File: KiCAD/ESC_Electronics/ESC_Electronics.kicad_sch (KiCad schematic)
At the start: 68 parts, among them J1 Batt probe, J10 RV Prob, J2 CA probe, J3 Test Input BNC, J4 -1000VDC SHV, J5 Output BNC, J6 Barrel_Jack, J7 DC Power, J8 -8V, J9 +8V, U1 CR110, U2 SiPhotodiode, U3 TL051CP, U4 LM317L, U5 UA78M08, U6 UA79M08, U7 TLE2426xP

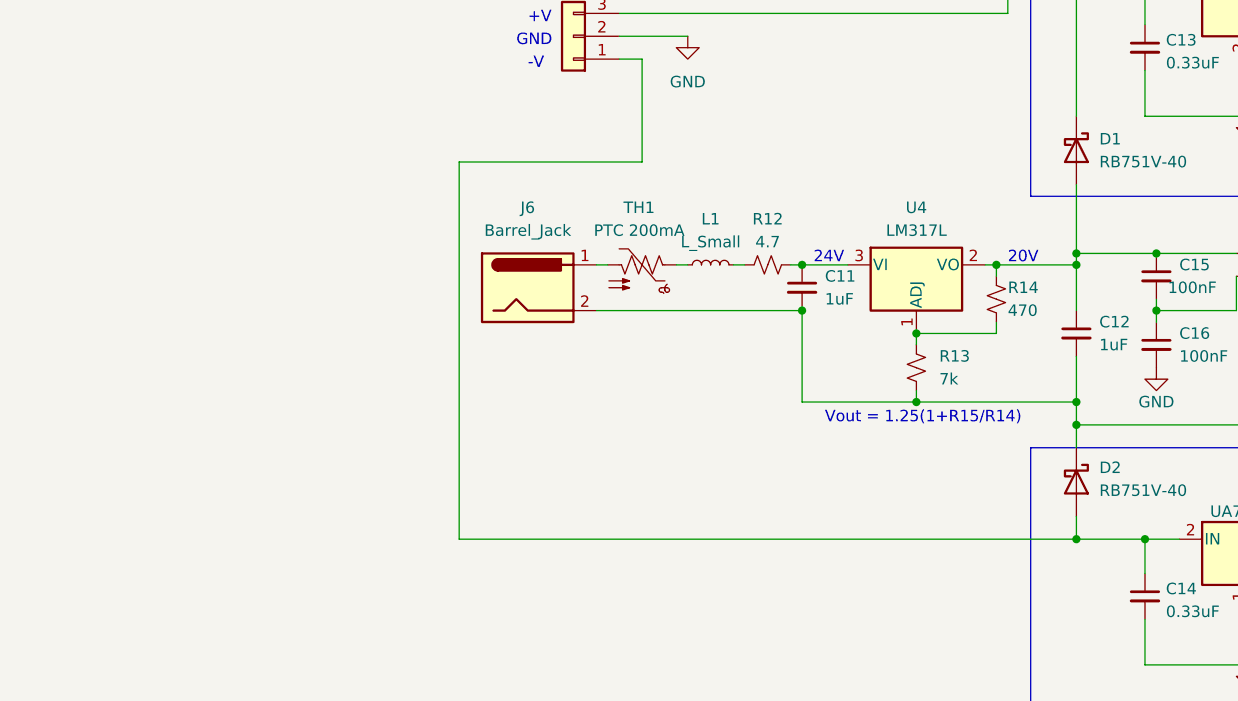
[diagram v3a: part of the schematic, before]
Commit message: Cleaning up SCH w/ notes
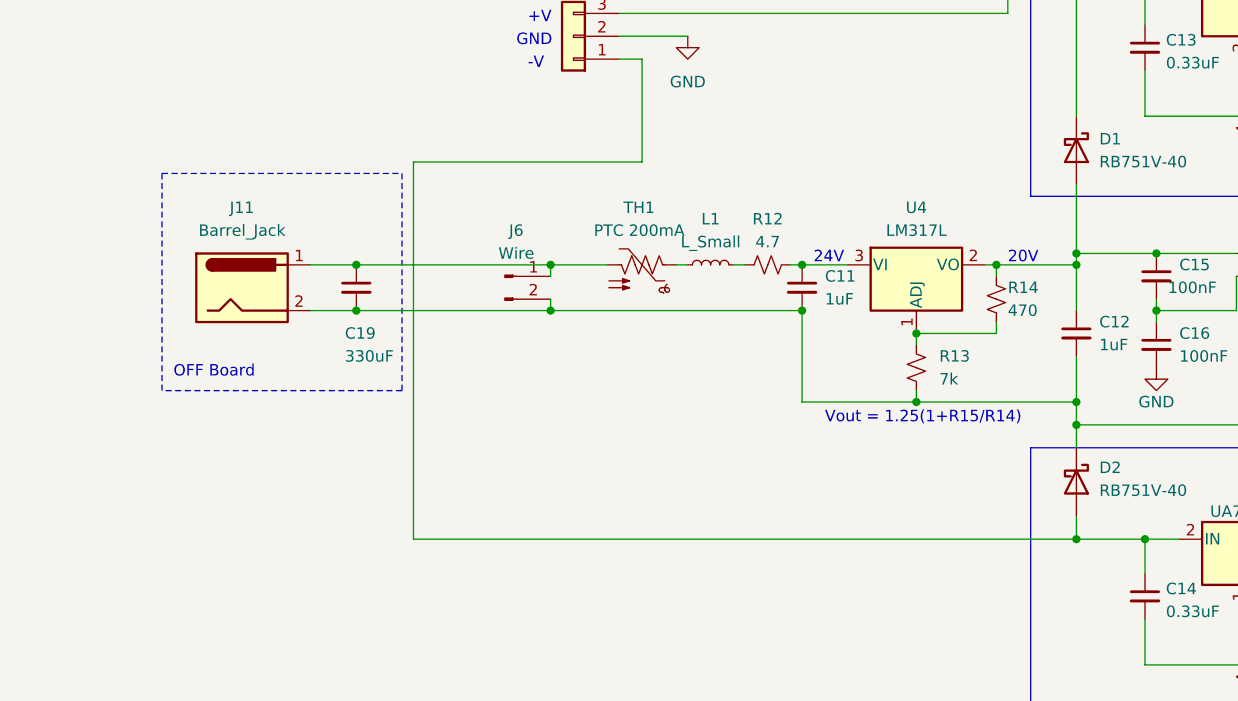
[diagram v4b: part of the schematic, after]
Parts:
- added C19: 330uF, symbol Device:C_Small
- added J11: Barrel_Jack, Connector_PinHeader_2.54mm:PinHeader_1x02_P2.54mm_Vertical, symbol Connector:Barrel_Jack
- J6: value Barrel_Jack -> Wire; symbol Connector:Barrel_Jack -> Connector:Conn_01x02_Pin; Digikey 839-1580-ND -> (none)
- R3: Digikey HVA05FA10M0CT-ND -> HVA12FA10M0CT-ND
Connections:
- net at J6.1 (Pin_1), TH1.2: now also C19.1, J11.1
- net at C11.2, C12.2, D2.1 (K)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: now also C19.2, J11.2
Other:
- note added: "OFF Board"
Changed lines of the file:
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@@
   (junction (at 127 102.87) (diameter 0) (color 0 0 0 0)
   )
+  (junction (at 257.81 119.38) (diameter 0) (color 0 0 0 0)
+  )
+  (junction (at 236.22 114.3) (diameter 0) (color 0 0 0 0)
+  )
   (junction (at 167.64 158.75) (diameter 0) (color 0 0 0 0)
   )
@@
   (junction (at 118.11 182.88) (diameter 0) (color 0 0 0 0)
   )
+  (junction (at 236.22 119.38) (diameter 0) (color 0 0 0 0)
+  )
+  (junction (at 257.81 114.3) (diameter 0) (color 0 0 0 0)
+  )
   (junction (at 323.85 144.78) (diameter 0) (color 0 0 0 0)
   )
@@
     (stroke (width 0) (type default))
   )
+  (wire (pts (xy 236.22 119.38) (xy 257.81 119.38))
+    (stroke (width 0) (type default))
+  )
   (wire (pts (xy 323.85 153.67) (xy 323.85 158.75))
     (stroke (width 0) (type default))
   )
+  (polyline (pts (xy 241.3 104.14) (xy 241.3 128.27))
+    (stroke (width 0) (type dash))
+  )
   (wire (pts (xy 325.12 119.38) (xy 334.01 119.38))
     (stroke (width 0) (type default))
@@
     (stroke (width 0) (type default))
   )
+  (polyline (pts (xy 214.63 128.27) (xy 214.63 104.14))
+    (stroke (width 0) (type dash))
+  )
   (wire (pts (xy 102.87 162.56) (xy 111.76 162.56))
     (stroke (width 0) (type default))
@@
     (stroke (width 0) (type default))
   )
+  (wire (pts (xy 231.14 114.3) (xy 236.22 114.3))
+    (stroke (width 0) (type default))
+  )
   (wire (pts (xy 316.23 113.03) (xy 316.23 114.3))
     (stroke (width 0) (type default))
@@
     (stroke (width 0) (type default))
   )
+  (wire (pts (xy 257.81 114.3) (xy 257.81 115.57))
+    (stroke (width 0) (type default))
+  )
   (wire (pts (xy 316.23 113.03) (xy 325.12 113.03))
     (stroke (width 0) (type default))
@@
     (stroke (width 0) (type default))
   )
+  (wire (pts (xy 236.22 114.3) (xy 257.81 114.3))
+    (stroke (width 0) (type default))
+  )
   (wire (pts (xy 185.42 180.34) (xy 185.42 182.88))
     (stroke (width 0) (type default))
@@
     (stroke (width 0) (type default))
   )
+  (wire (pts (xy 242.57 144.78) (xy 316.23 144.78))
+    (stroke (width 0) (type default))
+  )
   (wire (pts (xy 111.76 102.87) (xy 114.3 102.87))
     (stroke (width 0) (type default))
@@
     (stroke (width 0) (type default))
   )
-  (wire (pts (xy 247.65 144.78) (xy 247.65 102.87))
+  (wire (pts (xy 242.57 144.78) (xy 242.57 102.87))
     (stroke (width 0) (type default))
   )
@@
     (stroke (width 0) (type default))
   )
-  (wire (pts (xy 262.89 114.3) (xy 264.16 114.3))
+  (wire (pts (xy 257.81 114.3) (xy 264.16 114.3))
     (stroke (width 0) (type default))
   )
@@
     (stroke (width 0) (type default))
   )
+  (polyline (pts (xy 241.3 128.27) (xy 214.63 128.27))
+    (stroke (width 0) (type dash))
+  )
   (wire (pts (xy 193.04 162.56) (xy 193.04 173.99))
     (stroke (width 0) (type default))
@@
     (stroke (width 0) (type default))
   )
+  (polyline (pts (xy 214.63 104.14) (xy 241.3 104.14))
+    (stroke (width 0) (type dash))
+  )
   (wire (pts (xy 350.52 163.83) (xy 350.52 144.78))
     (stroke (width 0) (type default))
@@
     (stroke (width 0) (type default))
   )
+  (wire (pts (xy 257.81 118.11) (xy 257.81 119.38))
+    (stroke (width 0) (type default))
+  )
   (polyline (pts (xy 82.55 137.16) (xy 144.78 137.16))
     (stroke (width 0) (type default))
@@
     (stroke (width 0) (type default))
   )
-  (wire (pts (xy 247.65 144.78) (xy 316.23 144.78))
-    (stroke (width 0) (type default))
-  )
   (wire (pts (xy 347.98 163.83) (xy 350.52 163.83))
     (stroke (width 0) (type default))
@@
     (stroke (width 0) (type default))
   )
-  (wire (pts (xy 267.97 102.87) (xy 247.65 102.87))
+  (wire (pts (xy 242.57 102.87) (xy 267.97 102.87))
     (stroke (width 0) (type default))
   )
@@
     (stroke (width 0) (type default))
   )
+  (wire (pts (xy 231.14 119.38) (xy 236.22 119.38))
+    (stroke (width 0) (type default))
+  )
   (wire (pts (xy 342.9 83.82) (xy 344.17 83.82))
     (stroke (width 0) (type default))
@@
     (stroke (width 0) (type default))
   )
-  (wire (pts (xy 262.89 119.38) (xy 285.75 119.38))
+  (wire (pts (xy 257.81 119.38) (xy 285.75 119.38))
     (stroke (width 0) (type default))
   )
@@
   )
   (text "-10V" (at 339.09 132.08 0)
+    (effects (font (size 1.27 1.27)) (justify left bottom))
+  )
+  (text "OFF Board" (at 215.9 127 0)
     (effects (font (size 1.27 1.27)) (justify left bottom))
   )
@@
       (effects (font (size 1.27 1.27)) hide)
     )
-    (property "Datasheet" "https://www.digikey.com/en/products/detail/stackpole-electronics-inc/HVA05FA10M0/6195853" (at 118.11 121.92 0)
-      (effects (font (size 1.27 1.27)) hide)
-    )
-    (property "Digikey" "HVA05FA10M0CT-ND" (at 118.11 121.92 90)
+    (property "Datasheet" "https://www.digikey.com/en/products/detail/stackpole-electronics-inc/HVA12FA10M0/6195859?s=N4IgTCBcDaIBIDUCCBGMAxVAGAslgwgCoC0AcgCIgC6AvkA" (at 118.11 121.92 0)
+      (effects (font (size 1.27 1.27)) hide)
+    )
+    (property "Digikey" "HVA12FA10M0CT-ND" (at 118.11 121.92 90)
       (effects (font (size 1.27 1.27)) hide)
     )
@@
     )
   )
-  (symbol (lib_id "Connector:Barrel_Jack") (at 255.27 116.84 0) (unit 1)
-    (in_bom yes) (on_board yes) (dnp no) (fields_autoplaced)
-    (property "Reference" "J6" (at 255.27 107.95 0)
-      (effects (font (size 1.27 1.27)))
-    )
-    (property "Value" "Barrel_Jack" (at 255.27 110.49 0)
-      (effects (font (size 1.27 1.27)))
-    )
-    (property "Footprint" "Connector_PinHeader_2.54mm:PinHeader_1x02_P2.54mm_Vertical" (at 256.54 117.856 0)
-      (effects (font (size 1.27 1.27)) hide)
-    )
-    (property "Datasheet" "https://www.digikey.com/en/products/detail/tensility-international-corp/54-00151/9829987" (at 256.54 117.856 0)
-      (effects (font (size 1.27 1.27)) hide)
-    )
-    (property "Digikey" "839-1580-ND" (at 255.27 116.84 0)
+  (symbol (lib_id "Connector:Conn_01x02_Pin") (at 252.73 115.57 0) (unit 1)
+    (in_bom yes) (on_board yes) (dnp no)
+    (property "Reference" "J6" (at 254 110.49 0)
+      (effects (font (size 1.27 1.27)))
+    )
+    (property "Value" "Wire" (at 254 113.03 0)
+      (effects (font (size 1.27 1.27)))
+    )
+    (property "Footprint" "Connector_PinHeader_2.54mm:PinHeader_1x02_P2.54mm_Vertical" (at 252.73 115.57 0)
+      (effects (font (size 1.27 1.27)) hide)
+    )
+    (property "Datasheet" "" (at 252.73 115.57 0)
+      (effects (font (size 1.27 1.27)) hide)
+    )
+    (property "Digikey" "" (at 252.73 115.57 0)
       (effects (font (size 1.27 1.27)) hide)
     )
@@
     )
   )
+  (symbol (lib_id "Connector:Barrel_Jack") (at 223.52 116.84 0) (unit 1)
+    (in_bom yes) (on_board no) (dnp no) (fields_autoplaced)
+    (property "Reference" "J11" (at 223.52 107.95 0)
+      (effects (font (size 1.27 1.27)))
+    )
+    (property "Value" "Barrel_Jack" (at 223.52 110.49 0)
+      (effects (font (size 1.27 1.27)))
+    )
+    (property "Footprint" "Connector_PinHeader_2.54mm:PinHeader_1x02_P2.54mm_Vertical" (at 224.79 117.856 0)
+      (effects (font (size 1.27 1.27)) hide)
+    )
+    (property "Datasheet" "https://www.digikey.com/en/products/detail/tensility-international-corp/54-00151/9829987" (at 224.79 117.856 0)
+      (effects (font (size 1.27 1.27)) hide)
+    )
+    (property "Digikey" "839-1580-ND" (at 223.52 116.84 0)
+      (effects (font (size 1.27 1.27)) hide)
+    )
+    (pin "1")
+    (pin "2")
+    (instances
+      (project "ESC_Electronics"
+        (path "/b2dc06cf-e263-43ae-a5ba-6696795c1bac"
+          (reference "J11") (unit 1)
+        )
+      )
+    )
+  )
   (symbol (lib_id "Device:R_Potentiometer_US") (at 158.75 158.75 270) (unit 1)
     (in_bom yes) (on_board yes) (dnp no) (fields_autoplaced)
@@
         )
       )
+    )
+  )
+  (symbol (lib_id "Device:C_Small") (at 236.22 116.84 0) (unit 1)
+    (in_bom yes) (on_board no) (dnp no)
+    (property "Reference" "C19" (at 234.95 121.92 0)
+      (effects (font (size 1.27 1.27)) (justify left))
+    )
+    (property "Value" "330uF" (at 234.95 124.46 0)
+      (effects (font (size 1.27 1.27)) (justify left))
+    )
+    (property "Footprint" "" (at 236.22 116.84 0)
+      (effects (font (size 1.27 1.27)) hide)
+    )
+    (property "Datasheet" "https://www.digikey.com/en/products/detail/panasonic-electronic-components/ECA-2AM331/245069" (at 236.22 116.84 0)
+      (effects (font (size 1.27 1.27)) hide)
+    )
+    (property "Digikey" "P5315-ND" (at 236.22 116.84 0)
+      (effects (font (size 1.27 1.27)) hide)
+    )
+    (pin "1")
+    (pin "2")
+    (instances
+      (project "ESC_Electronics"
+        (path "/b2dc06cf-e263-43ae-a5ba-6696795c1bac"
+          (reference "C19") (unit 1)
+        )
+      )

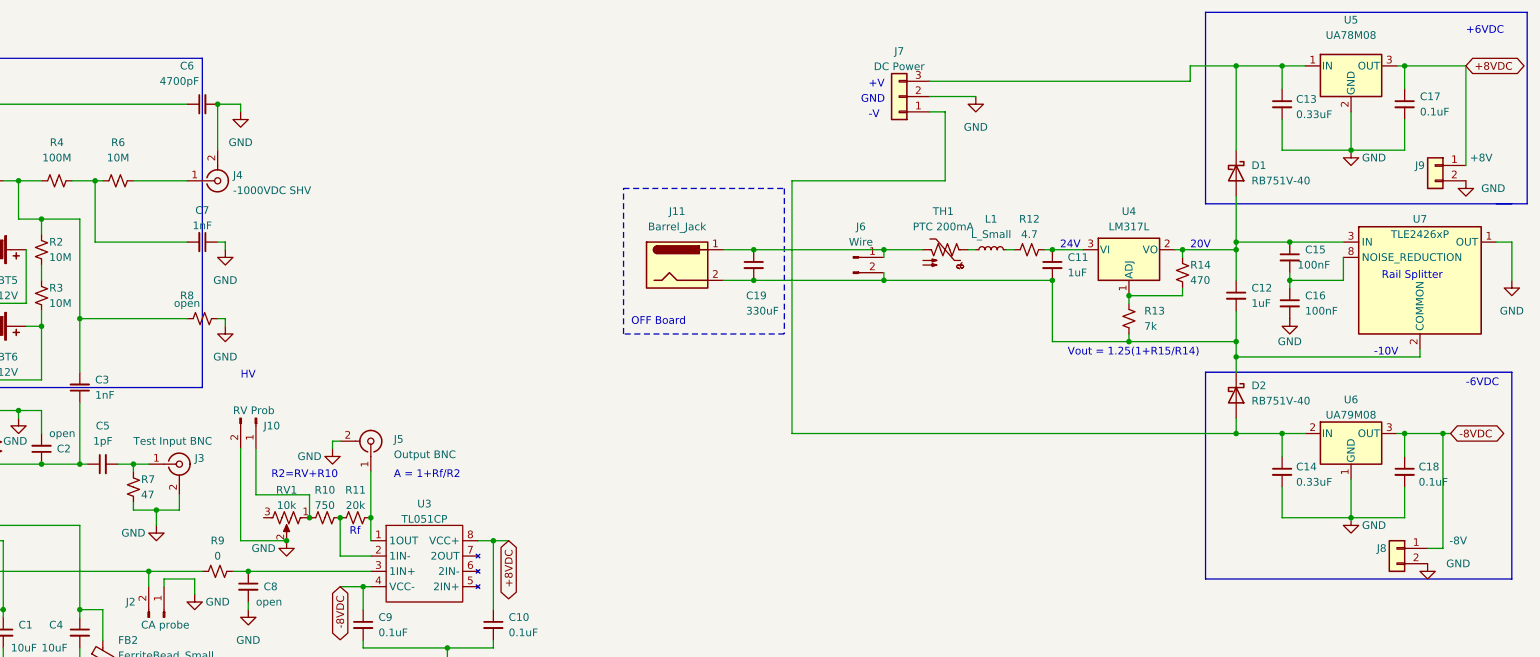
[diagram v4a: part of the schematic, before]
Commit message: Modification for external PS
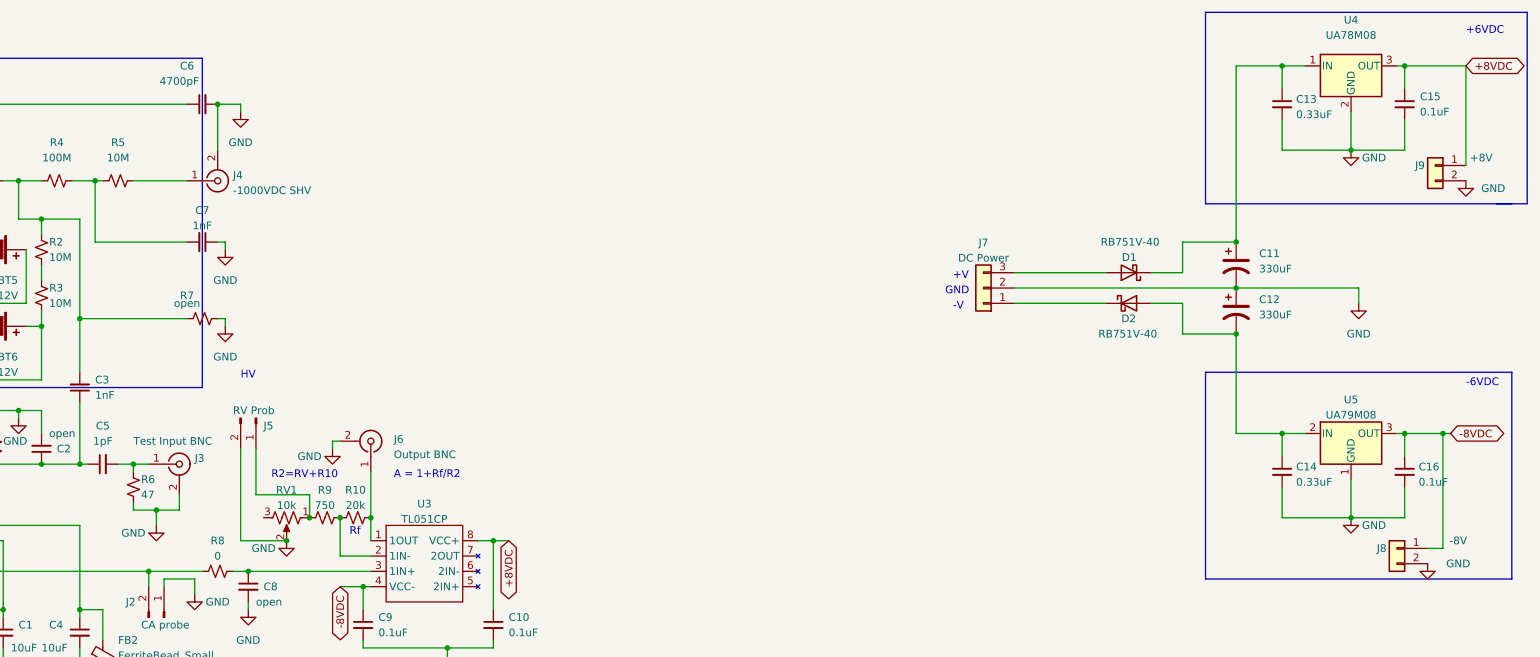
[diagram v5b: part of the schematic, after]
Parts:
- removed C11, C12: 1uF, Capacitor_SMD:C_0805_2012Metric_Pad1.18x1.45mm_HandSolder, symbol Device:C_Small
- removed C15, C16: 100nF, Capacitor_SMD:C_0805_2012Metric_Pad1.18x1.45mm_HandSolder, symbol Device:C_Small
- removed C19: 330uF, symbol Device:C_Small
- removed J11: Barrel_Jack, Connector_PinHeader_2.54mm:PinHeader_1x02_P2.54mm_Vertical, symbol Connector:Barrel_Jack
- removed J6: Wire, Connector_PinHeader_2.54mm:PinHeader_1x02_P2.54mm_Vertical, symbol Connector:Conn_01x02_Pin
- removed L1: L_Small, Inductor_THT:L_Radial_D7.0mm_P3.00mm, symbol Device:L_Small
- removed R12: 4.7, Resistor_SMD:R_2512_6332Metric_Pad1.40x3.35mm_HandSolder, symbol Device:R_Small_US
- removed R13: 7k, Resistor_SMD:R_0805_2012Metric_Pad1.20x1.40mm_HandSolder, symbol Device:R_Small_US
- removed R14: 470, Resistor_SMD:R_0805_2012Metric_Pad1.20x1.40mm_HandSolder, symbol Device:R_Small_US
- removed TH1: PTC 200mA, Fuse:Fuse_1210_3225Metric_Pad1.42x2.65mm_HandSolder, symbol Device:Thermistor_PTC_US
- removed U4: LM317L, Package_TO_SOT_SMD:SOT-89-3_Handsoldering, symbol Regulator_Linear:LM317_TO-220
- removed U7: TLE2426xP, Package_SO:SOIC-8_3.9x4.9mm_P1.27mm, symbol Reference_Voltage:TLE2426xD
- added C11, C12: 330uF, Capacitor_THT:CP_Radial_D10.0mm_P5.00mm, symbol Device:C_Polarized_US
- D1, D2: footprint Diode_SMD:D_SOD-323_HandSoldering -> Diode_SMD:D_SOD-123; Digikey 3757-RB751V-40-AU_R1_000A1CT-ND -> MBR0540TPMSCT-ND
- J7: footprint Connector_PinHeader_2.54mm:PinHeader_1x03_P2.54mm_Vertical -> Connector_Molex:Molex_KK-254_AE-6410-03A_1x03_P2.54mm_Vertical
- renumbered C17 to C15, C18 to C16, J10 to J5, J5 to J6, R11 to R10, R6 to R5, R7 to R6, R8 to R7, R9 to R8, R10 to R9, U5 to U4, U6 to U5
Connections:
- net GND: now also C11.2, C12.1
- net at C14.1, D2.2 (A), U5.2 (IN): now also C12.2; no longer J7.1 (Pin_1)
- net at C13.1, D1.1 (K), U4.1 (IN): now also C11.1; no longer J7.3 (Pin_3)
- net at D2.1 (K): now also J7.1 (Pin_1)
- net at D1.2 (A): now also J7.3 (Pin_3)
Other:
- note removed: "-10V"
- note removed: "20V"
- note removed: "24V"
- note removed: "OFF Board"
- note removed: "Rail Splitter"
- note removed: "Vout = 1.25(1+R15/R14)"
- moved on the sheet: D1, D2, J7

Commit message: Updating docs
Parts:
- C11, C12: Digikey (none) -> 1189-1766-ND
- J7: Digikey N/A -> WM4825-ND
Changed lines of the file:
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@@
       (effects (font (size 1.27 1.27)) hide)
     )
-    (property "Datasheet" "" (at 274.32 120.65 0)
-      (effects (font (size 1.27 1.27)) hide)
-    )
-    (property "Digikey" "N/A" (at 274.32 120.65 0)
+    (property "Datasheet" "https://www.digikey.com/en/products/detail/molex/0705430037/313740" (at 274.32 120.65 0)
+      (effects (font (size 1.27 1.27)) hide)
+    )
+    (property "Digikey" "WM4825-ND" (at 274.32 120.65 0)
       (effects (font (size 1.27 1.27)) hide)
     )
@@
       (effects (font (size 1.27 1.27)) hide)
     )
+    (property "Digikey" "1189-1766-ND" (at 316.23 124.46 0)
+      (effects (font (size 1.27 1.27)) hide)
+    )
     (pin "1")
     (pin "2")
@@
       (effects (font (size 1.27 1.27)) hide)
     )
+    (property "Digikey" "1189-1766-ND" (at 316.23 116.84 0)
+      (effects (font (size 1.27 1.27)) hide)
+    )
